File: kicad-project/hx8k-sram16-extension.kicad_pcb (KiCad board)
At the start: 2 copper layers, 32 x 54.3 mm, 24 parts, among them J1 Conn_01x06_Female, J2 Conn_01x06_Female, J3 Conn_02x20_Odd_Even, J4 Conn_02x20_Odd_Even, J5 Conn_01x06_Female, SW1 SW_Push, U1 fpga_shield2_IS61LV25616, U2 W25Q32JVSS

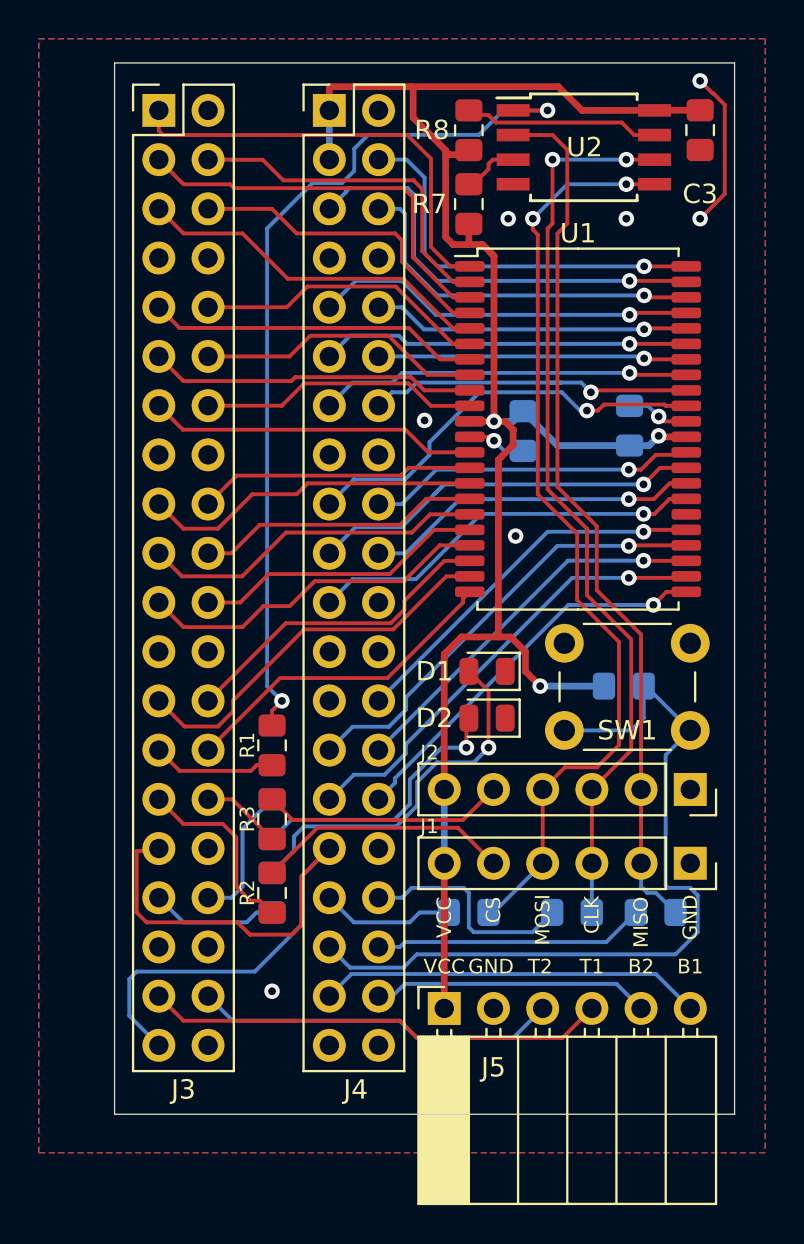
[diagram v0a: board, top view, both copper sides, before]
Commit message: switch to four layers
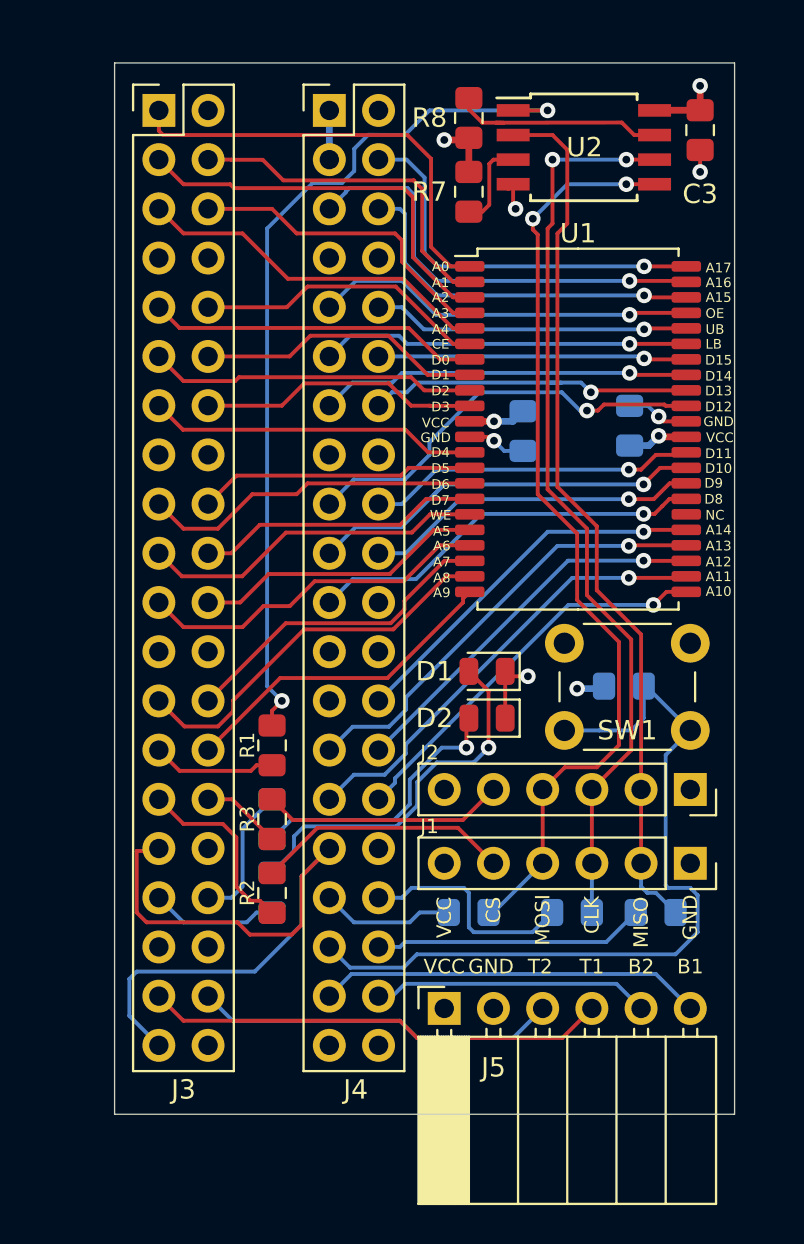
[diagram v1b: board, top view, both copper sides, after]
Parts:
- moved R7 0.63 mm to (92.2, 80.4), turned to 270 degrees
- moved R8 0.63 mm to (92.2, 76.6)
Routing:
- net VCC33: track 99.7 -> 17.3 mm, vias 3 -> 5
- net GND: track 51.2 -> 49.5 mm, vias 9 -> 5
- net Net-(R7-Pad2): track 3.07 -> 4.64 mm
- net Net-(R8-Pad2): track 10.0 -> 11.1 mm
- added copper zone on In1.Cu, net GND
- added copper zone on In2.Cu, net VCC33
- removed copper zone on B.Cu, net GND
- removed copper zone on F.Cu, net GND
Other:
- copper layers 2 -> 4
- board text added: "A0"
- board text added: "A1"
- board text added: "A10"
- board text added: "A11"
- board text added: "A12"
- board text added: "A13"
- board text added: "A14"
- board text added: "A15"
- board text added: "A16"
- board text added: "A17"
- board text added: "A2"
- board text added: "A3"
- board text added: "A4"
- board text added: "A5"
- board text added: "A6"
- board text added: "A7"
- board text added: "A8"
- board text added: "A9"
- board text added: "CE"
- board text added: "D0"
- board text added: "D1"
- board text added: "D10"
- board text added: "D11"
- board text added: "D12"
- board text added: "D13"
- board text added: "D14"
- board text added: "D15"
- board text added: "D2"
- board text added: "D3"
- board text added: "D4"
- board text added: "D5"
- board text added: "D6"
- board text added: "D7"
- board text added: "D8"
- board text added: "D9"
- board text added: "LB"
- board text added: "NC"
- board text added: "OE"
- board text added: "Rev. 3.0"
- board text added: "UB"
- board text added: "WE"
- board text removed: "Rev. 2.1"
